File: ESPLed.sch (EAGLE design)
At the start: 20 parts, among them IC1 TLC59711

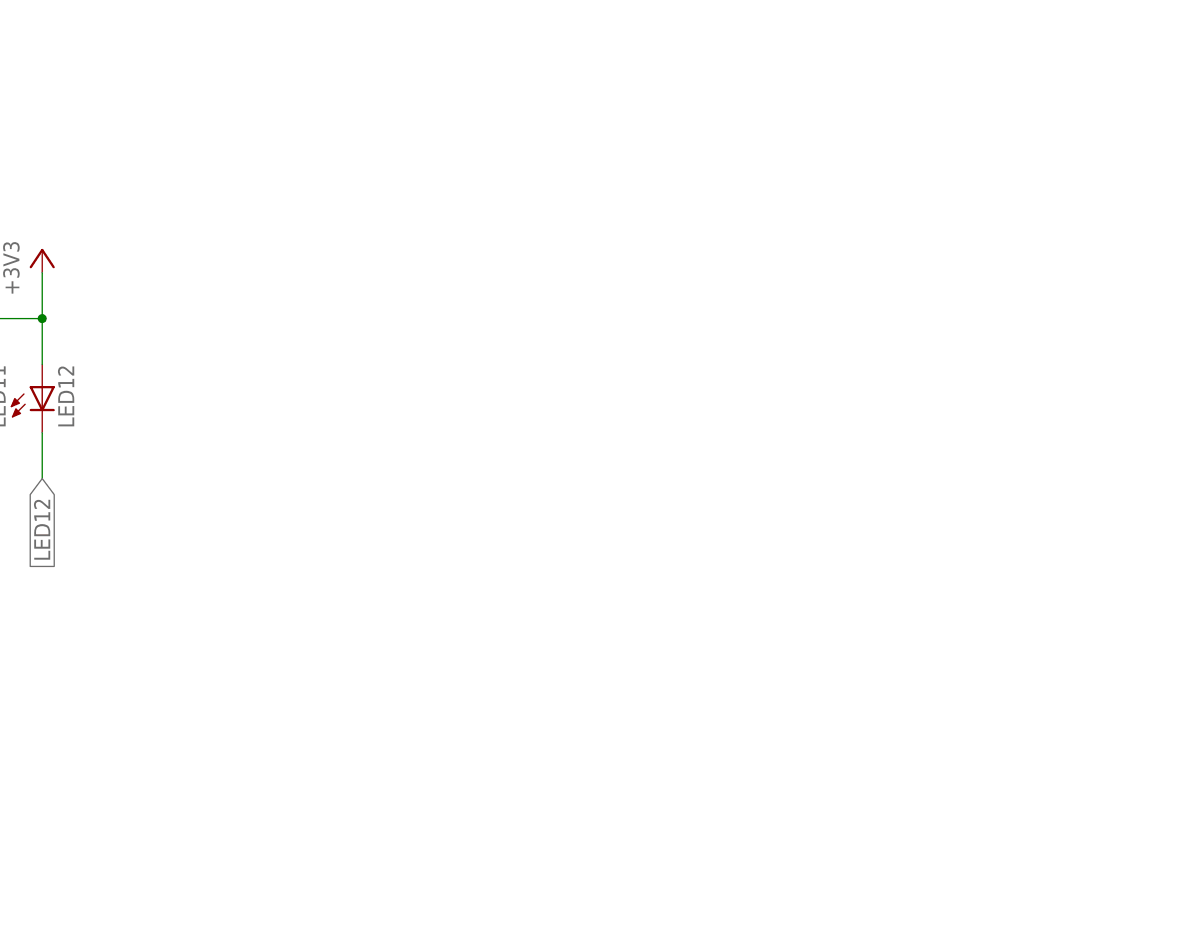
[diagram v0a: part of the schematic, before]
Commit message: buttons, usb
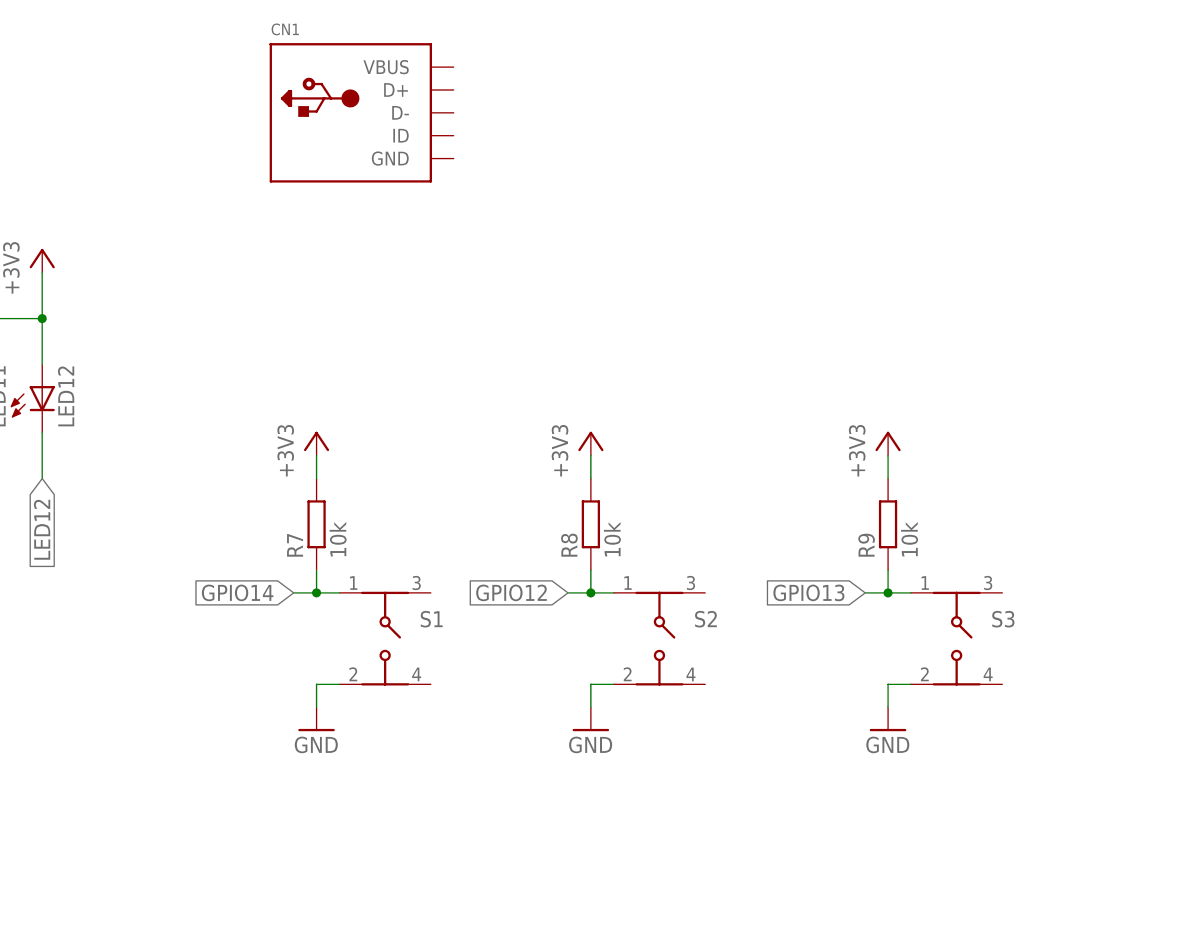
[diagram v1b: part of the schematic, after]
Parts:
- added CN1: (no value), adafruit:USBMINIB
- added R7, R8, R9: 10k, resistor:R-EU_R0805
- added S1, S2, S3: (no value), Wurth_Elektronik_Electromechanic_Switch_rev17b:4301X6XXX7X6_430156043726
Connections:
- net +3V3: now also R7.2, R8.2, R9.2
- net GND: now also S1.2, S2.2, S3.2
- net GPIO12: now also R8.1, S2.1
- net GPIO13: now also R9.1, S3.1
- net GPIO14: now also R7.1, S1.1
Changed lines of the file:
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@@
 <part name="+3V4" library="supply1" library_urn="urn:adsk.eagle:library:371" deviceset="+3V3" device=""/>
 <part name="R6" library="resistor" library_urn="urn:adsk.eagle:library:348" deviceset="R-EU_" device="R0805" value="1.98k"/>
+<part name="S1" library="Wurth_Elektronik_Electromechanic_Switch_rev17b" library_urn="urn:adsk.eagle:library:443" deviceset="4301X6XXX7X6" device="" technology="_430156043726"/>
+<part name="S2" library="Wurth_Elektronik_Electromechanic_Switch_rev17b" library_urn="urn:adsk.eagle:library:443" deviceset="4301X6XXX7X6" device="" technology="_430156043726"/>
+<part name="S3" library="Wurth_Elektronik_Electromechanic_Switch_rev17b" library_urn="urn:adsk.eagle:library:443" deviceset="4301X6XXX7X6" device="" technology="_430156043726"/>
+<part name="GND3" library="supply1" library_urn="urn:adsk.eagle:library:371" deviceset="GND" device=""/>
+<part name="GND5" library="supply1" library_urn="urn:adsk.eagle:library:371" deviceset="GND" device=""/>
+<part name="GND6" library="supply1" library_urn="urn:adsk.eagle:library:371" deviceset="GND" device=""/>
+<part name="R7" library="resistor" library_urn="urn:adsk.eagle:library:348" deviceset="R-EU_" device="R0805" value="10k"/>
+<part name="R8" library="resistor" library_urn="urn:adsk.eagle:library:348" deviceset="R-EU_" device="R0805" value="10k"/>
+<part name="R9" library="resistor" library_urn="urn:adsk.eagle:library:348" deviceset="R-EU_" device="R0805" value="10k"/>
+<part name="+3V5" library="supply1" library_urn="urn:adsk.eagle:library:371" deviceset="+3V3" device=""/>
+<part name="+3V6" library="supply1" library_urn="urn:adsk.eagle:library:371" deviceset="+3V3" device=""/>
+<part name="+3V7" library="supply1" library_urn="urn:adsk.eagle:library:371" deviceset="+3V3" device=""/>
+<part name="CN1" library="adafruit" library_urn="urn:adsk.eagle:library:420" deviceset="USB" device="MINIB"/>
 </parts>
 <sheets>
@@
 <instance part="+3V4" gate="G$1" x="236.22" y="66.04"/>
 <instance part="R6" gate="G$1" x="182.88" y="53.34"/>
+<instance part="S1" gate="G$1" x="137.16" y="96.52"/>
+<instance part="S2" gate="G$1" x="167.64" y="96.52"/>
+<instance part="S3" gate="G$1" x="200.66" y="96.52"/>
+<instance part="GND3" gate="1" x="129.54" y="86.36"/>
+<instance part="GND5" gate="1" x="160.02" y="86.36"/>
+<instance part="GND6" gate="1" x="193.04" y="86.36"/>
+<instance part="R7" gate="G$1" x="129.54" y="109.22" rot="R90"/>
+<instance part="R8" gate="G$1" x="160.02" y="109.22" rot="R90"/>
+<instance part="R9" gate="G$1" x="193.04" y="109.22" rot="R90"/>
+<instance part="+3V5" gate="G$1" x="129.54" y="119.38"/>
+<instance part="+3V6" gate="G$1" x="160.02" y="119.38"/>
+<instance part="+3V7" gate="G$1" x="193.04" y="119.38"/>
+<instance part="CN1" gate="G$1" x="134.62" y="154.94"/>
 </instances>
 <busses>
@@
 <wire x1="236.22" y1="53.34" x2="228.6" y2="53.34" width="0.1524" layer="91"/>
 </segment>
+<segment>
+<pinref part="R7" gate="G$1" pin="2"/>
+<wire x1="129.54" y1="114.3" x2="129.54" y2="116.84" width="0.1524" layer="91"/>
+<pinref part="+3V5" gate="G$1" pin="+3V3"/>
+</segment>
+<segment>
+<pinref part="R8" gate="G$1" pin="2"/>
+<wire x1="160.02" y1="114.3" x2="160.02" y2="116.84" width="0.1524" layer="91"/>
+<pinref part="+3V6" gate="G$1" pin="+3V3"/>
+</segment>
+<segment>
+<pinref part="R9" gate="G$1" pin="2"/>
+<wire x1="193.04" y1="114.3" x2="193.04" y2="116.84" width="0.1524" layer="91"/>
+<pinref part="+3V7" gate="G$1" pin="+3V3"/>
+</segment>
 </net>
 <net name="GND" class="0">
@@
 <junction x="170.18" y="53.34"/>
 </segment>
+<segment>
+<pinref part="S1" gate="G$1" pin="2"/>
+<wire x1="132.08" y1="91.44" x2="129.54" y2="91.44" width="0.1524" layer="91"/>
+<wire x1="129.54" y1="91.44" x2="129.54" y2="88.9" width="0.1524" layer="91"/>
+<pinref part="GND3" gate="1" pin="GND"/>
+</segment>
+<segment>
+<pinref part="S2" gate="G$1" pin="2"/>
+<wire x1="162.56" y1="91.44" x2="160.02" y2="91.44" width="0.1524" layer="91"/>
+<wire x1="160.02" y1="91.44" x2="160.02" y2="88.9" width="0.1524" layer="91"/>
+<pinref part="GND5" gate="1" pin="GND"/>
+</segment>
+<segment>
+<pinref part="S3" gate="G$1" pin="2"/>
+<wire x1="195.58" y1="91.44" x2="193.04" y2="91.44" width="0.1524" layer="91"/>
+<wire x1="193.04" y1="91.44" x2="193.04" y2="88.9" width="0.1524" layer="91"/>
+<pinref part="GND6" gate="1" pin="GND"/>
+</segment>
 </net>
 <net name="GPIO13" class="0">
@@
 <label x="10.16" y="35.56" size="1.016" layer="95" rot="R180" xref="yes"/>
 </segment>
+<segment>
+<pinref part="S3" gate="G$1" pin="1"/>
+<wire x1="195.58" y1="101.6" x2="193.04" y2="101.6" width="0.1524" layer="91"/>
+<label x="190.5" y="101.6" size="1.778" layer="95" rot="R180" xref="yes"/>
+<wire x1="193.04" y1="101.6" x2="190.5" y2="101.6" width="0.1524" layer="91"/>
+<wire x1="193.04" y1="101.6" x2="193.04" y2="104.14" width="0.1524" layer="91"/>
+<junction x="193.04" y="101.6"/>
+<pinref part="R9" gate="G$1" pin="1"/>
+</segment>
 </net>
 <net name="GPIO12" class="0">
@@
 <label x="10.16" y="38.1" size="1.016" layer="95" rot="R180" xref="yes"/>
 </segment>
+<segment>
+<pinref part="S2" gate="G$1" pin="1"/>
+<wire x1="162.56" y1="101.6" x2="160.02" y2="101.6" width="0.1524" layer="91"/>
+<label x="157.48" y="101.6" size="1.778" layer="95" rot="R180" xref="yes"/>
+<wire x1="160.02" y1="101.6" x2="157.48" y2="101.6" width="0.1524" layer="91"/>
+<wire x1="160.02" y1="101.6" x2="160.02" y2="104.14" width="0.1524" layer="91"/>
+<junction x="160.02" y="101.6"/>
+<pinref part="R8" gate="G$1" pin="1"/>
+</segment>
 </net>
 <net name="GPIO14" class="0">
@@
 <label x="10.16" y="40.64" size="1.016" layer="95" rot="R180" xref="yes"/>
 </segment>
-</net>
+<segment>
+<pinref part="S1" gate="G$1" pin="1"/>
+<wire x1="132.08" y1="101.6" x2="129.54" y2="101.6" width="0.1524" layer="91"/>
+<label x="127" y="101.6" size="1.778" layer="95" rot="R180" xref="yes"/>
+<wire x1="129.54" y1="101.6" x2="127" y2="101.6" width="0.1524" layer="91"/>
+<wire x1="129.54" y1="101.6" x2="129.54" y2="104.14" width="0.1524" layer="91"/>
+<junction x="129.54" y="101.6"/>
+<pinref part="R7" gate="G$1" pin="1"/>
+</segment>
+</net>

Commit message: lipo charging
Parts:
- added C1, C2: 12pF, resistor:C-EUC0805
- added C4, C5, C7: 10µF, resistor:C-EUC0805
- added C6: 1µF, resistor:C-EUC0805
- added D4: MBR120, microbuilder:DIODE-SCHOTTKYSOD-123
- added IC2: MCP73831/OT, adafruit:MCP73831/OT
- added LED13: (no value), led:LEDSML0805
- added Q1: 12MHz, JonasLib:CX5032GB12000H0PESZZ
- added Q3: DMG3415U, microbuilder:MOSFET-P
- added R10: 2k, resistor:R-EU_R0805
- added R11: 680, resistor:R-EU_R0805
- added R13, R14: 100k, resistor:R-EU_R0805
- added U$1: CH340G, ch340g:CH340G
- added U3: AP2112-3.3, microbuilder:VREG_SOT23-5
- added X1: JSTPH, microbuilder:CON_JST_PH_2PIN
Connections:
- net N$1 renamed IREF
- net N$8 renamed GPIO5
- new net IN: C4.2, D4.C, Q3.S, R13.1, U3.IN
- new net N$1: LED13.C, R11.1
- new net PROG: IC2.PROG, R10.1
- new net STAT: IC2.STAT, R11.2
- new net USB_D+: CN1.D+, U$1.D+
- new net USB_D-: CN1.D-, U$1.D-
- new net USB_RX: U$1.RX, U1.TX
- new net USB_TX: U$1.TX, U1.RX
- new net VBAT: IC2.VBAT, Q3.D, X1.2
- new net VBUS: CN1.VBUS, D4.A, IC2.VDD, LED13.A, Q3.G, R14.2
- new net VREG_EN: R13.2, U3.EN
- new net XI: C2.2, Q1.1, U$1.XI
- new net XO: C1.2, Q1.2, U$1.XO
- net +3V3: now also C5.2, C6.2, C7.2, IC1G$1.VCC, U$1.V3, U$1.VCC, U3.OUT
- net GND: now also C1.1, C2.1, C4.1, C5.1, C6.1, C7.1, CN1.GND, IC2.VSS, R10.2, R14.1, U$1.GND, U3.GND, X1.1
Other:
- note added: "1.0K = 1000mA"
- note added: "10K = 100mA"
- note added: "2.0K = 500mA"
- note added: "5.0K = 200mA"
- note added: "POWER AND FILTERING"
